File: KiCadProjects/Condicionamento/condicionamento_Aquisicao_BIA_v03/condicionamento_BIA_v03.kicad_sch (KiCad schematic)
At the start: 33 parts, among them J1 alimentacao analogica, J2 sinais analogicos, J3 comunicacao / sinais digitais, J4 Vref, J5 sinais_condicionados, J6 Eletrodos, J7 alimetacao_Master, U1 AD828AN, U2 BluePill_STM32F103C, U3 BluePill_STM32F103C

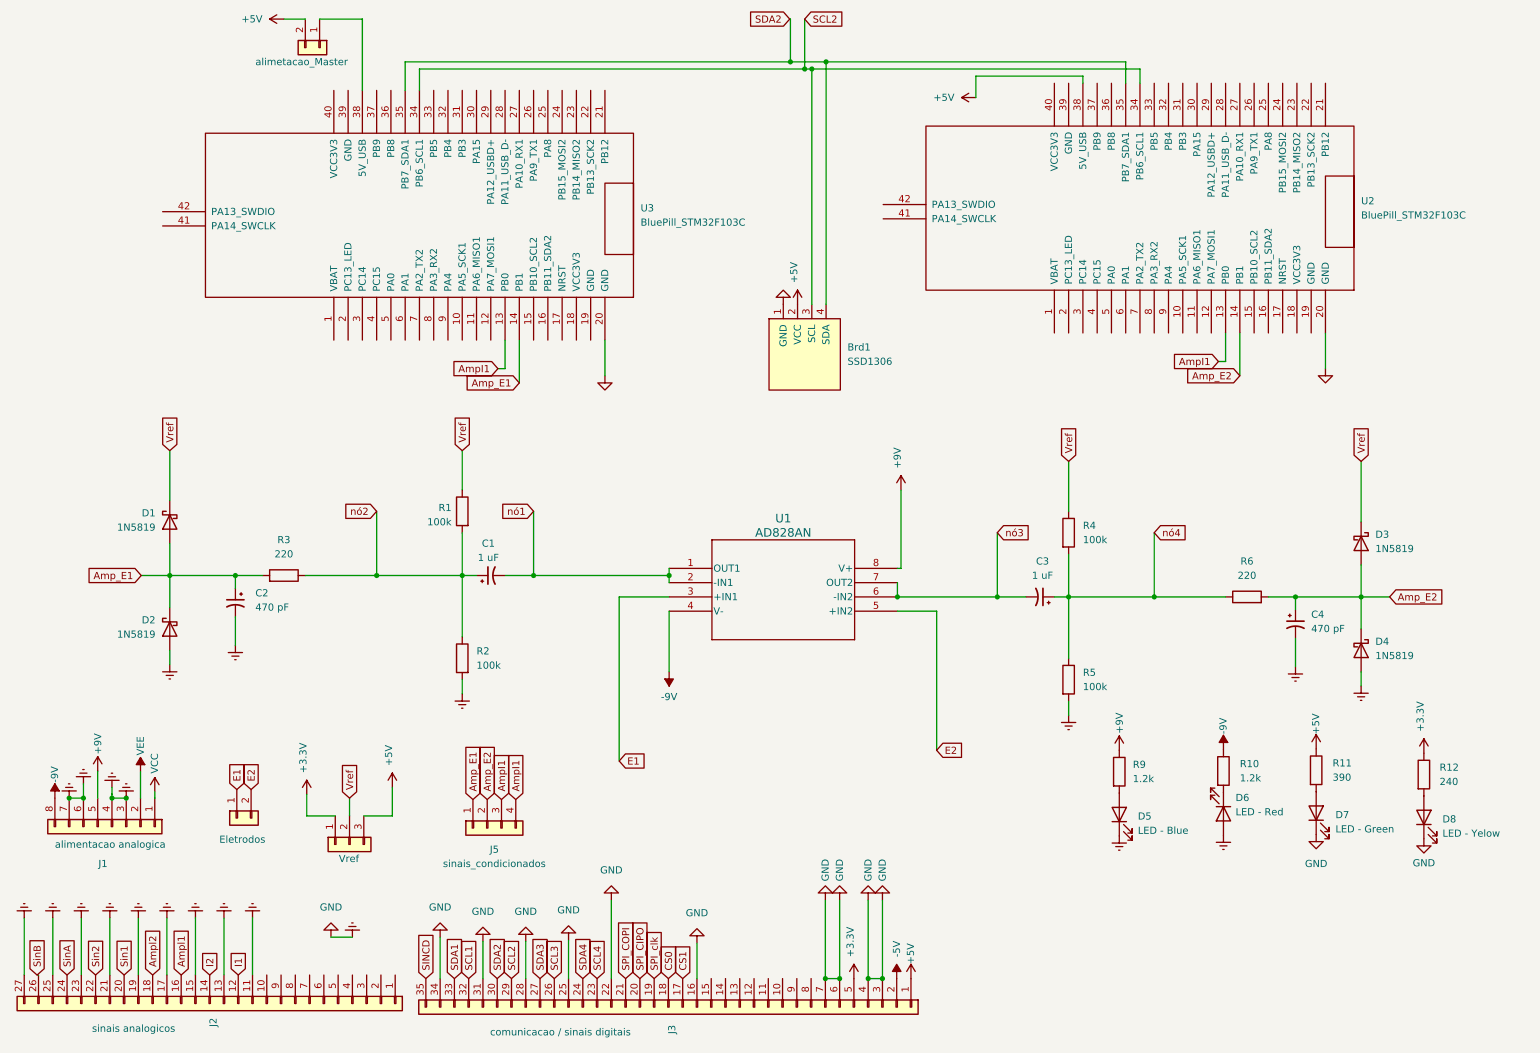
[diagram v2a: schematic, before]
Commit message: Baseado barramento v04 - Finalizado - implementacao resistor pullup i2c 2
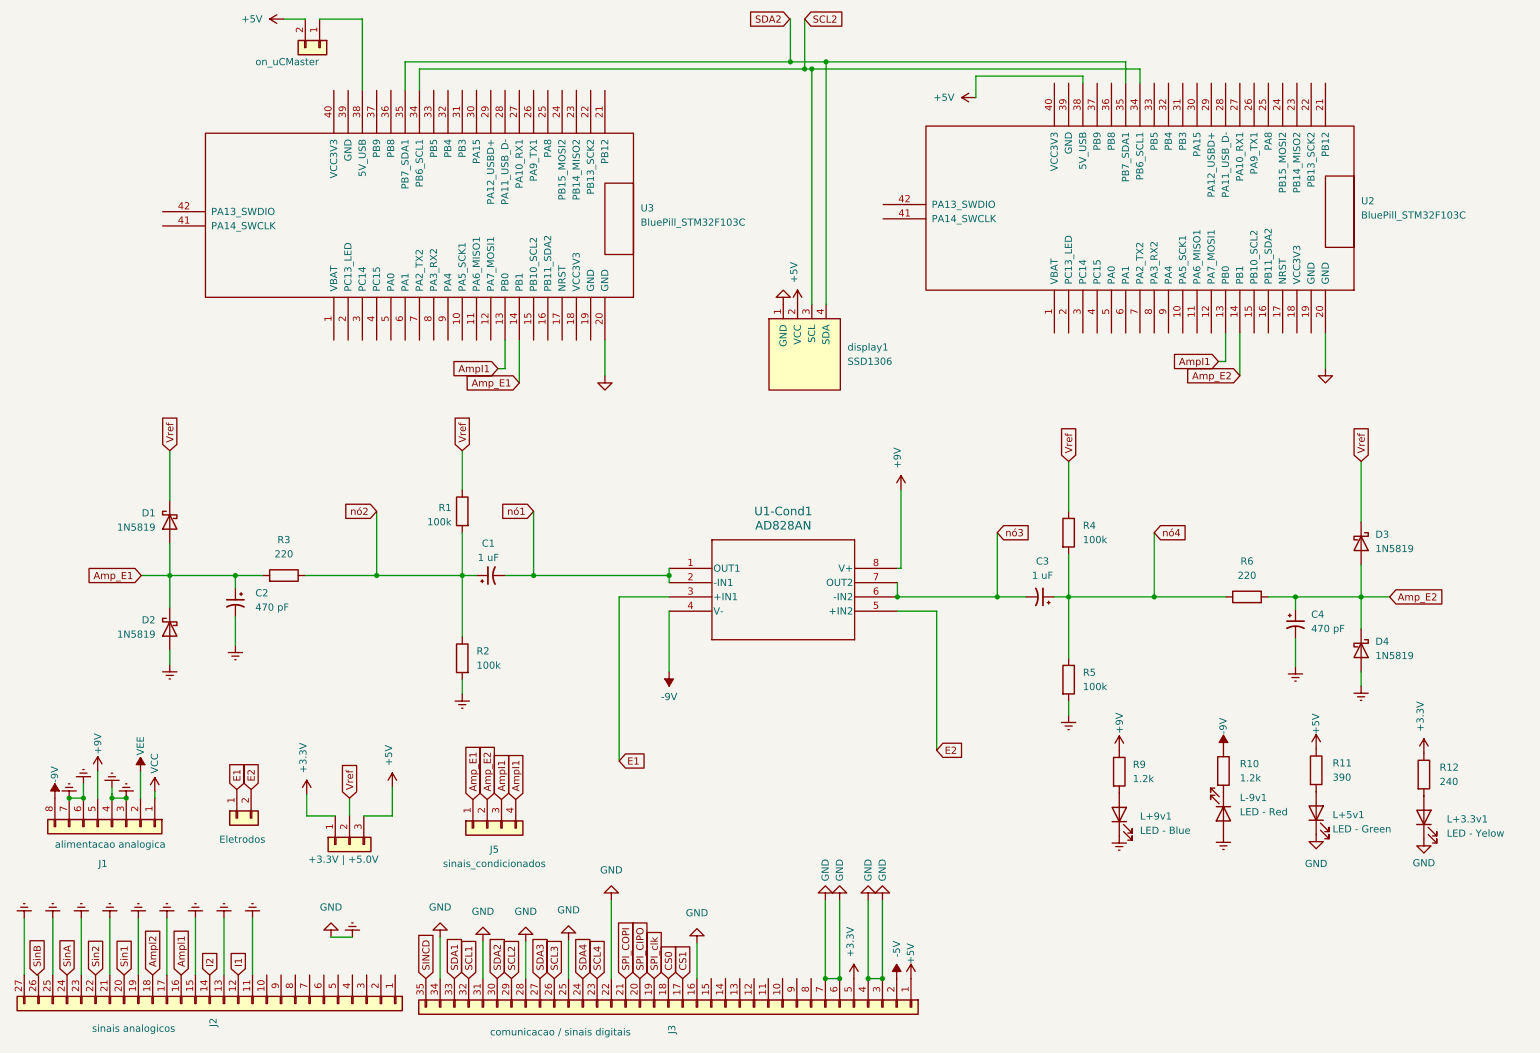
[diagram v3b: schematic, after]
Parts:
- J4: value Vref -> +3.3V | +5.0V
- J7: value alimetacao_Master -> on_uCMaster
- renumbered D8 to L+3.3v1, D7 to L+5v1, D5 to L+9v1, D6 to L-9v1, U1 to U1-Cond1, Brd1 to display1
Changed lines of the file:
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@@
   (symbol (lib_id "Device:LED") (at 228.219 155.448 270) (unit 1)
     (in_bom yes) (on_board yes) (dnp no) (fields_autoplaced)
-    (property "Reference" "D6" (at 230.378 152.5905 90)
-      (effects (font (size 1.27 1.27)) (justify left))
-    )
-    (property "Value" "LED - Red" (at 230.378 155.1305 90)
+    (property "Reference" "L-9v1" (at 231.14 152.5905 90)
+      (effects (font (size 1.27 1.27)) (justify left))
+    )
+    (property "Value" "LED - Red" (at 231.14 155.1305 90)
       (effects (font (size 1.27 1.27)) (justify left))
     )
@@
       (project "condicionamento_BIA_v03"
         (path "/f0ff92cf-26e5-4ab9-977d-5f9689e8a5d0"
-          (reference "D6") (unit 1)
+          (reference "L-9v1") (unit 1)
         )
       )
@@
       (effects (font (size 1.27 1.27)) (justify left) hide)
     )
-    (property "Value" "Vref" (at 70.739 163.449 90)
+    (property "Value" "+3.3V | +5.0V" (at 65.278 163.576 90)
       (effects (font (size 1.27 1.27)) (justify right))
     )
@@
   (symbol (lib_id "Device:LED") (at 244.729 155.321 90) (unit 1)
     (in_bom yes) (on_board yes) (dnp no) (fields_autoplaced)
-    (property "Reference" "D7" (at 248.158 155.6385 90)
+    (property "Reference" "L+5v1" (at 247.65 155.6385 90)
       (effects (font (size 1.27 1.27)) (justify right))
     )
-    (property "Value" "LED - Green" (at 248.158 158.1785 90)
+    (property "Value" "LED - Green" (at 247.65 158.1785 90)
       (effects (font (size 1.27 1.27)) (justify right))
     )
@@
       (project "condicionamento_BIA_v03"
         (path "/f0ff92cf-26e5-4ab9-977d-5f9689e8a5d0"
-          (reference "D7") (unit 1)
+          (reference "L+5v1") (unit 1)
         )
       )
@@
   (symbol (lib_id "SSD1306-128x64_OLED:SSD1306") (at 153.67 73.66 0) (unit 1)
     (in_bom yes) (on_board yes) (dnp no) (fields_autoplaced)
-    (property "Reference" "Brd1" (at 161.29 72.39 0)
+    (property "Reference" "display1" (at 161.29 72.39 0)
       (effects (font (size 1.27 1.27)) (justify left))
     )
@@
       (project "condicionamento_BIA_v03"
         (path "/f0ff92cf-26e5-4ab9-977d-5f9689e8a5d0"
-          (reference "Brd1") (unit 1)
+          (reference "display1") (unit 1)
         )
       )
@@
   (symbol (lib_id "AD828AN:AD828AN") (at 129.54 111.76 0) (unit 1)
     (in_bom yes) (on_board yes) (dnp no) (fields_autoplaced)
-    (property "Reference" "U1" (at 149.86 102.87 0)
+    (property "Reference" "U1-Cond1" (at 149.86 101.6 0)
       (effects (font (size 1.524 1.524)))
     )
-    (property "Value" "AD828AN" (at 149.86 105.41 0)
+    (property "Value" "AD828AN" (at 149.86 104.14 0)
       (effects (font (size 1.524 1.524)))
     )
@@
       (project "condicionamento_BIA_v03"
         (path "/f0ff92cf-26e5-4ab9-977d-5f9689e8a5d0"
-          (reference "U1") (unit 1)
+          (reference "U1-Cond1") (unit 1)
         )
       )
@@
   (symbol (lib_id "Device:LED") (at 263.906 156.083 90) (unit 1)
     (in_bom yes) (on_board yes) (dnp no) (fields_autoplaced)
-    (property "Reference" "D8" (at 267.208 156.4005 90)
+    (property "Reference" "L+3.3v1" (at 267.97 156.4005 90)
       (effects (font (size 1.27 1.27)) (justify right))
     )
-    (property "Value" "LED - Yelow" (at 267.208 158.9405 90)
+    (property "Value" "LED - Yelow" (at 267.97 158.9405 90)
       (effects (font (size 1.27 1.27)) (justify right))
     )
@@
       (project "condicionamento_BIA_v03"
         (path "/f0ff92cf-26e5-4ab9-977d-5f9689e8a5d0"
-          (reference "D8") (unit 1)
+          (reference "L+3.3v1") (unit 1)
         )
       )
@@
   (symbol (lib_id "Device:LED") (at 209.677 155.575 90) (unit 1)
     (in_bom yes) (on_board yes) (dnp no) (fields_autoplaced)
-    (property "Reference" "D5" (at 212.979 155.8925 90)
+    (property "Reference" "L+9v1" (at 213.36 155.8925 90)
       (effects (font (size 1.27 1.27)) (justify right))
     )
-    (property "Value" "LED - Blue" (at 212.979 158.4325 90)
+    (property "Value" "LED - Blue" (at 213.36 158.4325 90)
       (effects (font (size 1.27 1.27)) (justify right))
     )
@@
       (project "condicionamento_BIA_v03"
         (path "/f0ff92cf-26e5-4ab9-977d-5f9689e8a5d0"
-          (reference "D5") (unit 1)
+          (reference "L+9v1") (unit 1)
         )
       )
@@
       (effects (font (size 1.27 1.27)) (justify left) hide)
     )
-    (property "Value" "alimetacao_Master" (at 55.88 21.59 90)
-      (effects (font (size 1.27 1.27)) (justify left))
-    )
+    (property "Value" "on_uCMaster" (at 55.88 21.59 90)
+      (effects (font (size 1.27 1.27)) (justify left))
+    )

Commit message: V03 em producao - Compacto em projeto
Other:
- title: Condicionamento e aquisicao 2 canais  -> Condicionamento BIA
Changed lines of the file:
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@@
   (paper "A4")
   (title_block
-    (title "Condicionamento e aquisicao 2 canais ")
-    (date "2023-07-17")
+    (title "Condicionamento BIA")
+    (date "2024-06-06")
     (rev "v03")
     (company "EITduino")
     (comment 1 "Autor: Gustavo Pinheiro")
-    (comment 2 "placa face dupla 90x100 mm")
+    (comment 2 "placa face dupla 100x100 mm")
     (comment 3 "Barramento V04")
+    (comment 4 "Condicionamento e aquisicao 2 canais ")
   )
   (junction (at 200.66 116.84) (diameter 0) (color 0 0 0 0)
